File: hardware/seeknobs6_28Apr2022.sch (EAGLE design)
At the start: 29 parts, among them SW1 SPST-6.0MM, SW2 SPST-6.0MM, SW3 SPST-6.0MM, SW4 SPST-6.0MM

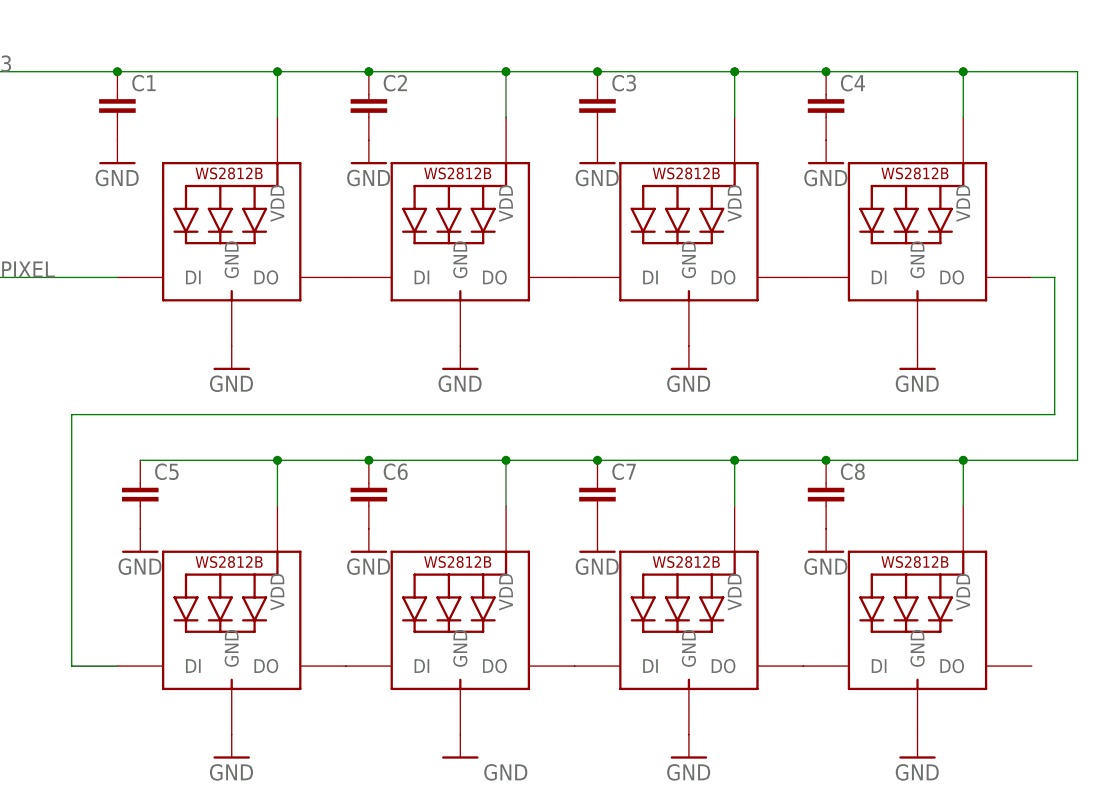
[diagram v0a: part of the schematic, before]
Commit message: doc updates, cirpy example
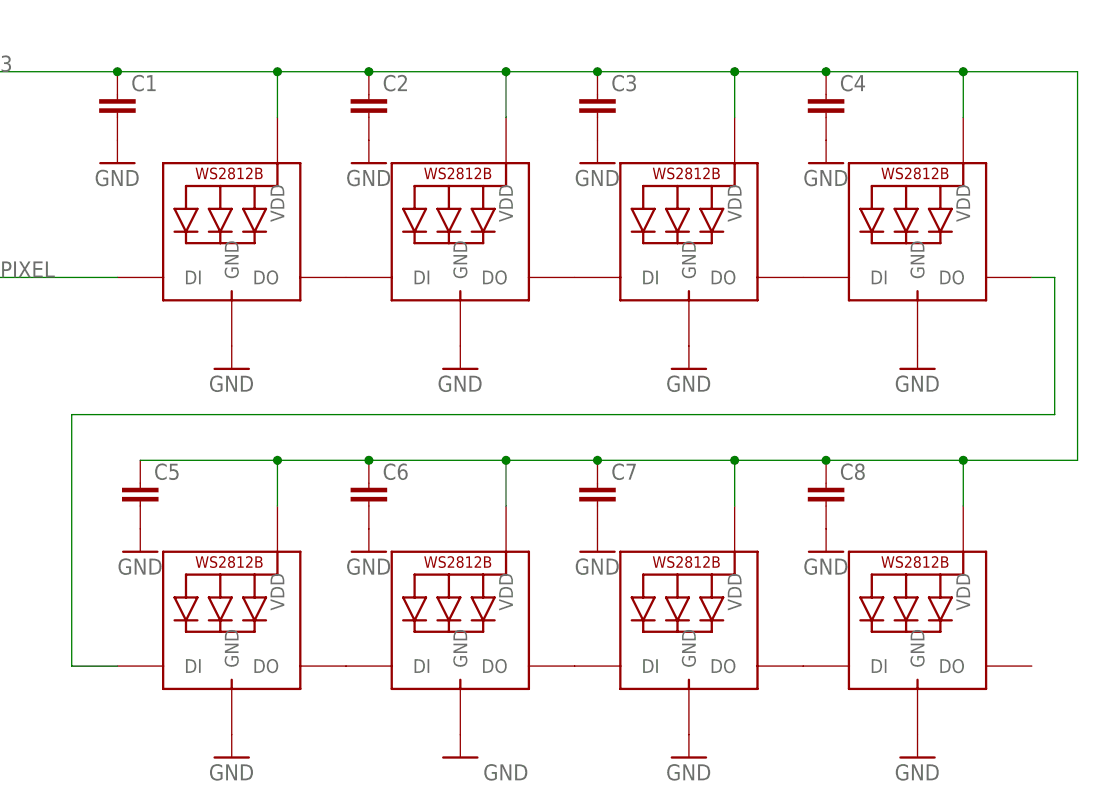
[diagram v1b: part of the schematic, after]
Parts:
- LED1, LED2, LED3, LED4, LED5, LED6, LED7, LED8: value MICROBUILDER_WS2812B5050 -> WS2812B5050EZ; device Adafruit MacroPad 2040:MICROBUILDER_WS2812B5050 -> todstuff:WS2812B5050EZ
